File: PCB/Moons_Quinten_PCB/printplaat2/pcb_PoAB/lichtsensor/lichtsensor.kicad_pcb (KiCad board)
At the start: 2 copper layers, 9.8 x 11.2 mm, 3 parts, among them J1 Conn_01x03_Male, Q1 TEMT6000X01

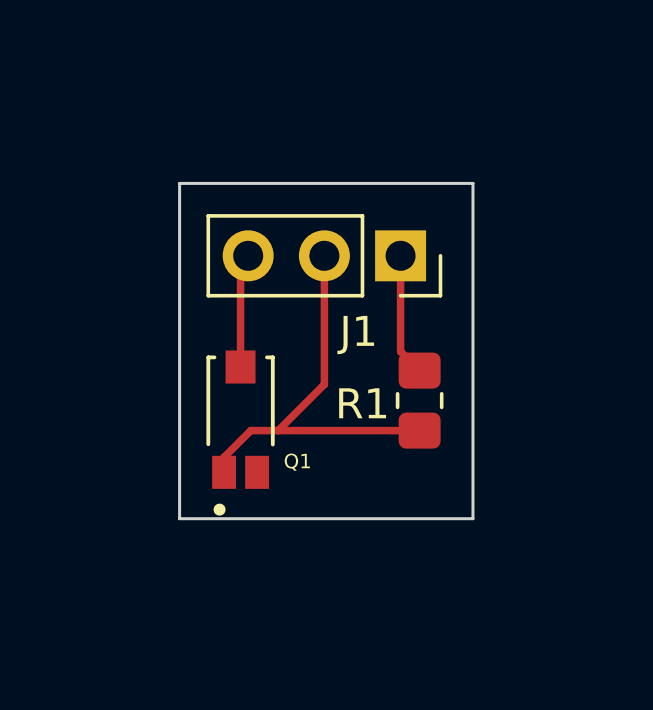
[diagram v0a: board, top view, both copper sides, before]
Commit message: printplaat en lichtmeter aangepast
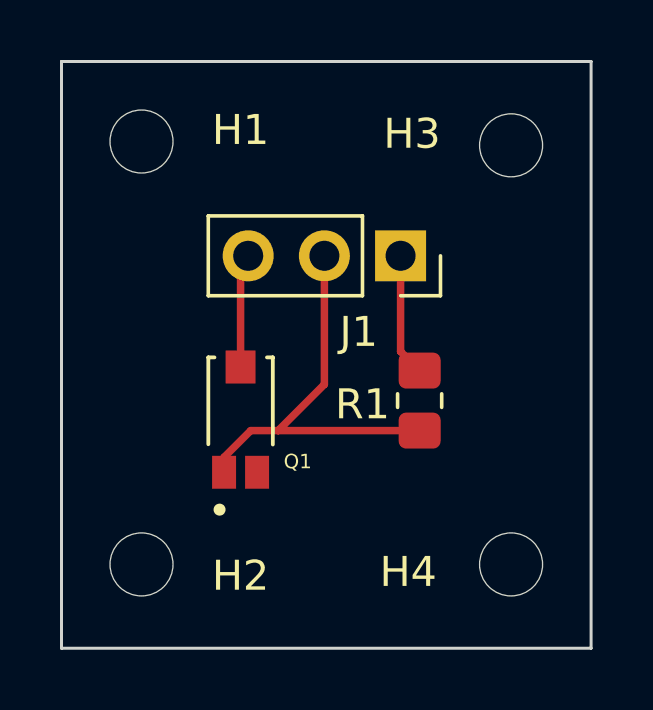
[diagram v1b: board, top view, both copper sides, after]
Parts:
- added H1: MountingHole_Pad, MountingHole:MountingHole_2.1mm, F.Cu at (129.0, 66.5)
- added H2: MountingHole_Pad, MountingHole:MountingHole_2.1mm, F.Cu at (129.0, 80.6)
- added H3: MountingHole_Pad, MountingHole:MountingHole_2.1mm, F.Cu at (141.4, 66.7)
- added H4: MountingHole_Pad, MountingHole:MountingHole_2.1mm, F.Cu at (141.4, 80.6)
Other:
- board size 9.8 x 11.2 mm -> 17.7 x 19.6 mm
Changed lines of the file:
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@@
   (net 2 "/output")
   (net 3 "VCC")
+  (footprint "MountingHole:MountingHole_2.1mm" (layer "F.Cu")
+    (at 141.351 66.675)
+    (descr "Mounting Hole 2.1mm, no annular")
+    (tags "mounting hole 2.1mm no annular")
+    (property "Sheetfile" "lichtsensor.kicad_sch")
+    (property "Sheetname" "")
+    (attr exclude_from_pos_files)
+    (fp_text reference "H3" (at -3.302 -0.381) (layer "F.SilkS")
+      (effects (font (size 1 1) (thickness 0.15)))
+    )
+    (fp_text value "MountingHole_Pad" (at 0 3.2) (layer "F.Fab")
+      (effects (font (size 1 1) (thickness 0.15)))
+    )
+    (fp_text user "${REFERENCE}" (at 0 0) (layer "F.Fab")
+      (effects (font (size 1 1) (thickness 0.15)))
+    )
+    (fp_circle (center 0 0) (end 2.1 0) (layer "Cmts.User") (width 0.15) (fill none))
+    (fp_circle (center 0 0) (end 2.35 0) (layer "F.CrtYd") (width 0.05) (fill none))
+    (pad "" np_thru_hole circle (at 0 0) (size 2.1 2.1) (drill 2.1) (layers *.Cu *.Mask))
+  )
+  (footprint "MountingHole:MountingHole_2.1mm" (layer "F.Cu")
+    (at 129.032 66.548)
+    (descr "Mounting Hole 2.1mm, no annular")
+    (tags "mounting hole 2.1mm no annular")
+    (property "Sheetfile" "lichtsensor.kicad_sch")
+    (property "Sheetname" "")
+    (attr exclude_from_pos_files)
+    (fp_text reference "H1" (at 3.302 -0.381) (layer "F.SilkS")
+      (effects (font (size 1 1) (thickness 0.15)))
+    )
+    (fp_text value "MountingHole_Pad" (at 0 3.2) (layer "F.Fab")
+      (effects (font (size 1 1) (thickness 0.15)))
+    )
+    (fp_text user "${REFERENCE}" (at 0 0) (layer "F.Fab")
+      (effects (font (size 1 1) (thickness 0.15)))
+    )
+    (fp_circle (center 0 0) (end 2.1 0) (layer "Cmts.User") (width 0.15) (fill none))
+    (fp_circle (center 0 0) (end 2.35 0) (layer "F.CrtYd") (width 0.05) (fill none))
+    (pad "" np_thru_hole circle (at 0 0) (size 2.1 2.1) (drill 2.1) (layers *.Cu *.Mask))
+  )
   (footprint "TEMT6000X01:TRANS_TEMT6000X01" (layer "F.Cu")
     (at 132.334 75.819 90)
@@
     )
   )
+  (footprint "MountingHole:MountingHole_2.1mm" (layer "F.Cu")
+    (at 129.032 80.645)
+    (descr "Mounting Hole 2.1mm, no annular")
+    (tags "mounting hole 2.1mm no annular")
+    (property "Sheetfile" "lichtsensor.kicad_sch")
+    (property "Sheetname" "")
+    (attr exclude_from_pos_files)
+    (fp_text reference "H2" (at 3.302 0.381) (layer "F.SilkS")
+      (effects (font (size 1 1) (thickness 0.15)))
+    )
+    (fp_text value "MountingHole_Pad" (at 0 3.2) (layer "F.Fab")
+      (effects (font (size 1 1) (thickness 0.15)))
+    )
+    (fp_text user "${REFERENCE}" (at 0 0) (layer "F.Fab")
+      (effects (font (size 1 1) (thickness 0.15)))
+    )
+    (fp_circle (center 0 0) (end 2.1 0) (layer "Cmts.User") (width 0.15) (fill none))
+    (fp_circle (center 0 0) (end 2.35 0) (layer "F.CrtYd") (width 0.05) (fill none))
+    (pad "" np_thru_hole circle (at 0 0) (size 2.1 2.1) (drill 2.1) (layers *.Cu *.Mask))
+  )
   (footprint "Connector_PinSocket_2.54mm:PinSocket_1x03_P2.54mm_Vertical" (layer "F.Cu")
     (at 137.668 70.358 -90)
@@
     )
   )
-  (gr_rect (start 130.302 67.945) (end 140.081 79.121) (layer "Edge.Cuts") (width 0.1) (fill none))
+  (footprint "MountingHole:MountingHole_2.1mm" (layer "F.Cu")
+    (at 141.351 80.645)
+    (descr "Mounting Hole 2.1mm, no annular")
+    (tags "mounting hole 2.1mm no annular")
+    (property "Sheetfile" "lichtsensor.kicad_sch")
+    (property "Sheetname" "")
+    (attr exclude_from_pos_files)
+    (fp_text reference "H4" (at -3.429 0.254) (layer "F.SilkS")
+      (effects (font (size 1 1) (thickness 0.15)))
+    )
+    (fp_text value "MountingHole_Pad" (at 0 3.2) (layer "F.Fab")
+      (effects (font (size 1 1) (thickness 0.15)))
+    )
+    (fp_text user "${REFERENCE}" (at 0 0) (layer "F.Fab")
+      (effects (font (size 1 1) (thickness 0.15)))
+    )
+    (fp_circle (center 0 0) (end 2.1 0) (layer "Cmts.User") (width 0.15) (fill none))
+    (fp_circle (center 0 0) (end 2.35 0) (layer "F.CrtYd") (width 0.05) (fill none))
+    (pad "" np_thru_hole circle (at 0 0) (size 2.1 2.1) (drill 2.1) (layers *.Cu *.Mask))
+  )
+  (gr_rect (start 126.365 63.881) (end 144.018 83.439) (layer "Edge.Cuts") (width 0.1) (fill none))
   (segment (start 137.668 70.358) (end 137.668 73.549) (width 0.25) (layer "F.Cu") (net 1))
   (segment (start 137.668 73.549) (end 138.303 74.184) (width 0.25) (layer "F.Cu") (net 1))
